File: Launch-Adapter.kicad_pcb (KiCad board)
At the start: 4 copper layers, 80.3 x 142.5 mm, 92 parts, among them J1 ADC1, J10 +5V_CAN, J11 Interfaces, J12 Current Measure, J13 Current Measure, J14 +5V, J2 ADC2, J3 PWM, J4 GPIO, J5 Driver, J6 Voltage measure, J7 +5V, J8 +15V, J9 +3.3V, Q1 BC817, U3 ISO1050DUB, U4 ADM3490ExR, U5 LMV324

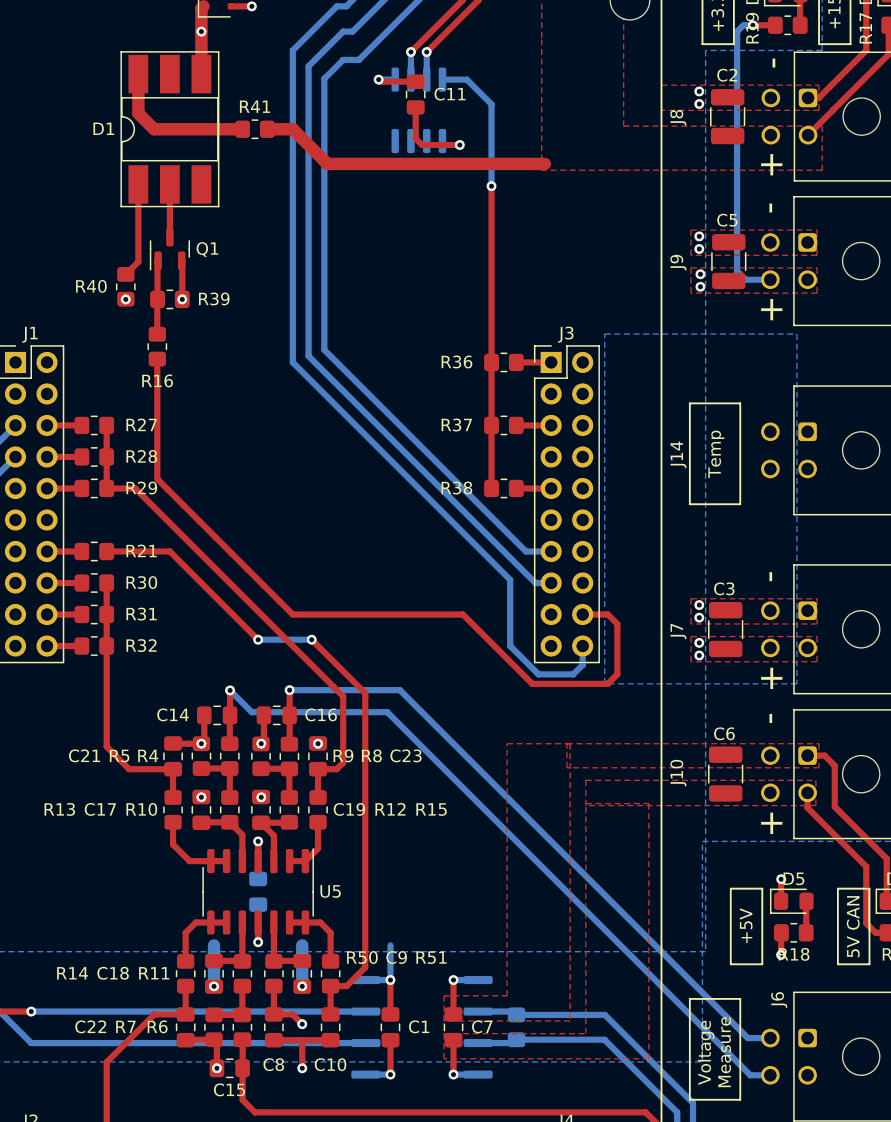
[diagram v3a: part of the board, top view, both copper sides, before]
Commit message: Поменял посадочное место резистора реле
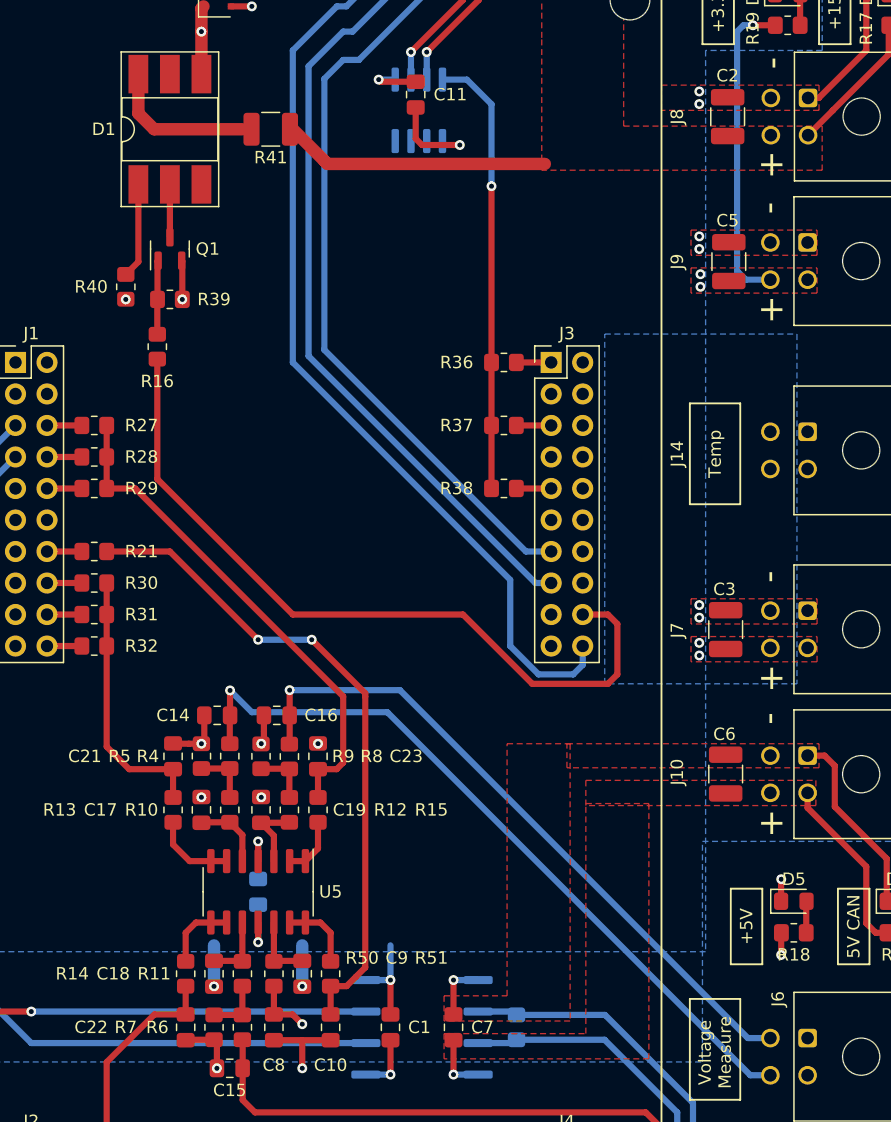
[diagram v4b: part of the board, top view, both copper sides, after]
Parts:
- R41: footprint Resistor_SMD:R_0805_2012Metric_Pad1.20x1.40mm_HandSolder -> Resistor_SMD:R_1210_3225Metric_Pad1.30x2.65mm_HandSolder
- moved R41 1.27 mm to (83.6, 45.0)
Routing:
- net +15V: track 35.1 -> 33.0 mm
